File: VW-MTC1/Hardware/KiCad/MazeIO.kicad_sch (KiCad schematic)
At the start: 21 parts, among them J4 MAZE, Q4 AO3400A, U10 TPD4E05U06, U11 74LVC3G17

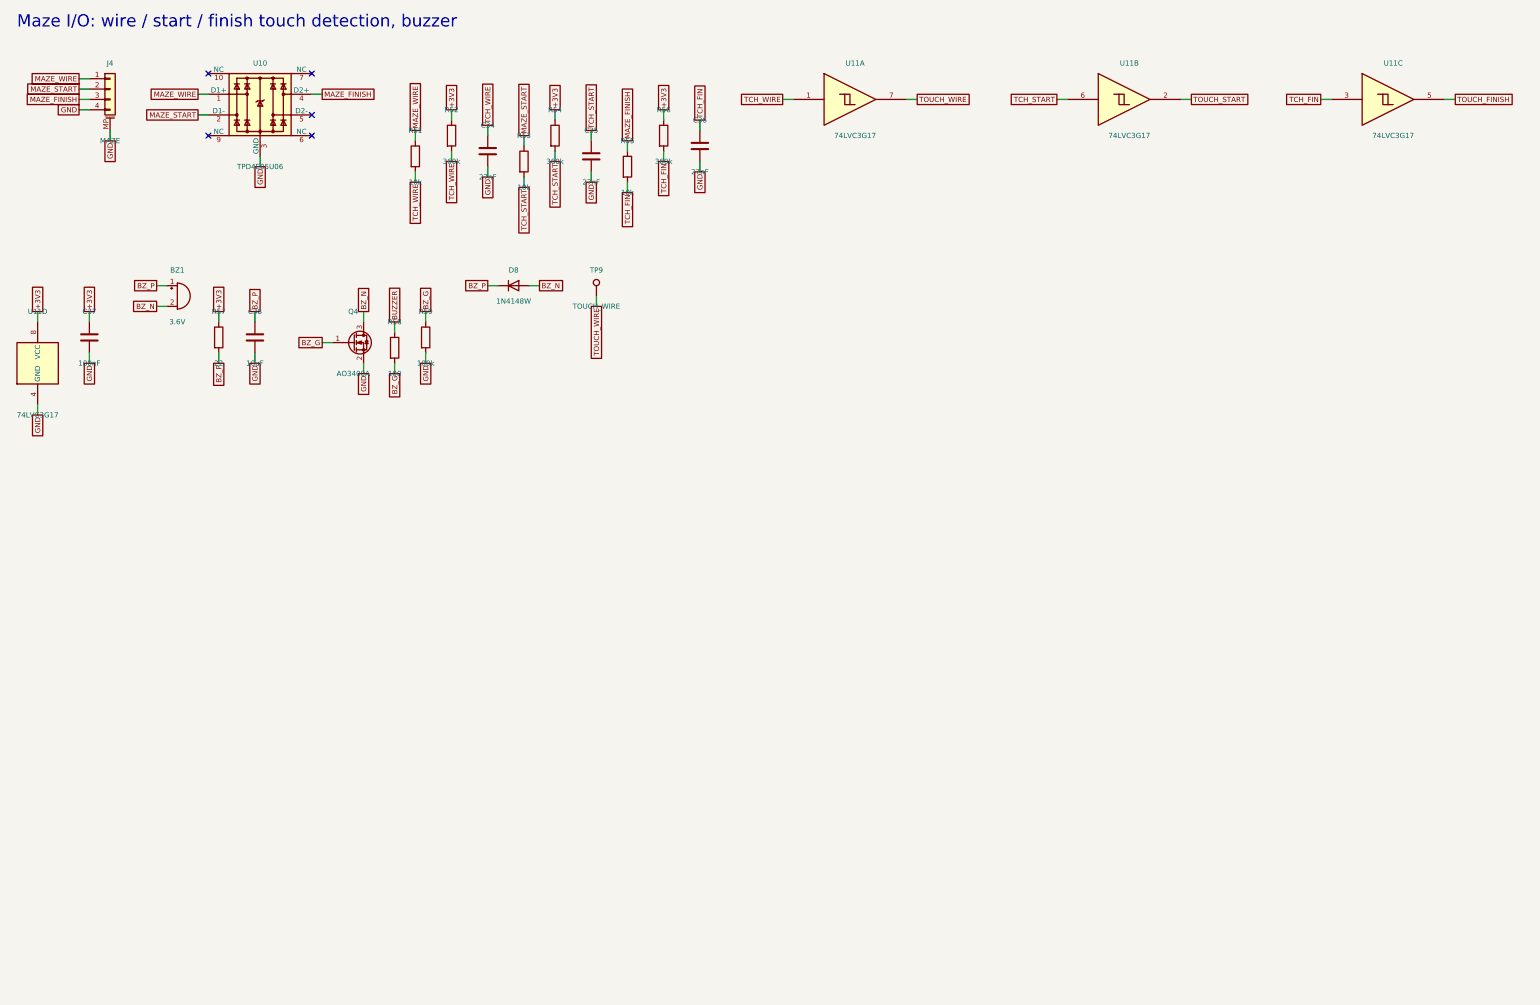
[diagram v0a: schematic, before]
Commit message: Apply Rev B touch circuit, routed PCB and topology-tested BOM
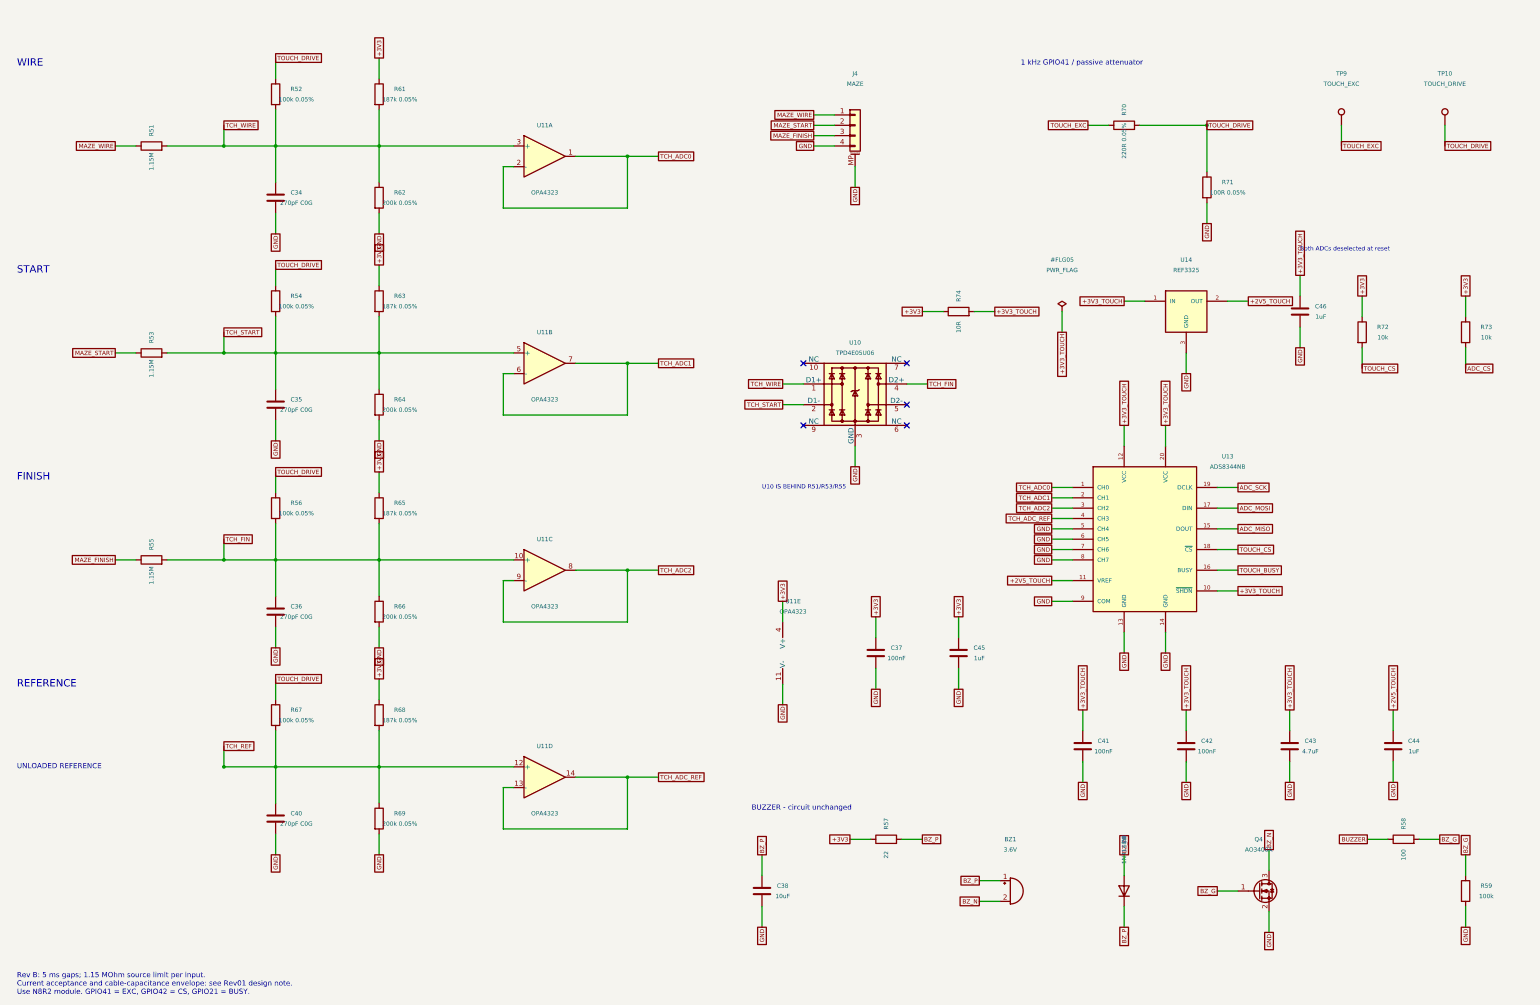
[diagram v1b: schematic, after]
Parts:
- removed U11: 74LVC3G17, Package_SO:VSSOP-8_2.3x2mm_P0.5mm, symbol 74xGxx:74LVC3G17
- added C40: 270pF C0G, Capacitor_SMD:C_0603_1608Metric, symbol Device:C
- added C41, C42: 100nF, Capacitor_SMD:C_0603_1608Metric, symbol Device:C
- added C43: 4.7uF, Capacitor_SMD:C_0603_1608Metric, symbol Device:C
- added C44, C45, C46: 1uF, Capacitor_SMD:C_0603_1608Metric, symbol Device:C
- added R61, R63, R65, R68: 187k 0.05%, Resistor_SMD:R_0603_1608Metric, symbol Device:R
- added R62, R64, R66, R69: 200k 0.05%, Resistor_SMD:R_0603_1608Metric, symbol Device:R
- added R67: 100k 0.05%, Resistor_SMD:R_0603_1608Metric, symbol Device:R
- added R70: 220R 0.05%, Resistor_SMD:R_0603_1608Metric, symbol Device:R
- added R71: 100R 0.05%, Resistor_SMD:R_0603_1608Metric, symbol Device:R
- added R72, R73: 10k, Resistor_SMD:R_0603_1608Metric, symbol Device:R
- added R74: 10R, Resistor_SMD:R_0603_1608Metric, symbol Device:R
- added TP10: TOUCH_DRIVE, TestPoint:TestPoint_Pad_D1.5mm, symbol Connector:TestPoint
- added U11: OPA4323, Package_SO:TSSOP-14_4.4x5mm_P0.65mm, symbol Voltwyn:OPA4323
- added U13: ADS8344NB, Package_SO:SSOP-20_5.3x7.2mm_P0.65mm, symbol Voltwyn:ADS8344NB
- added U14: REF3325, Package_TO_SOT_SMD:SOT-23, symbol Voltwyn:REF3325
- C34, C35, C36: value 27nF -> 270pF C0G; MPN GRM188R71H273KA01D -> GRM1885C1H271JA01D
- R51, R53, R55: value 10k -> 1.15M; MPN RC0603FR-0710kL -> RC0603FR-071M15L
- R52, R54, R56: value 360k -> 100k 0.05%; MPN RC0603FR-07360kL -> RG1608N-104-W-T1; Manufacturer Yageo -> Susumu
- TP9: value TOUCH_WIRE -> TOUCH_EXC
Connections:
- net +3V3: now also C45.1, R61.1, R63.1, R65.1, R68.1, R72.1, R73.1, R74.1, U11.4 (V+); no longer R52.1, R54.1, R56.1
- net GND: now also C40.2, C41.2, C42.2, C43.2, C44.2, C45.2, C46.2, R62.2, R64.2, R66.2, R69.2, R71.2, U11.11 (V-), U13.13 (GND), U13.14 (GND), U13.5 (CH4), U13.6 (CH5), U13.7 (CH6), U13.8 (CH7), U13.9 (COM), U14.3 (GND)
- net MAZE_FINISH: no longer U10.4 (D2+)
- net MAZE_START: no longer U10.2 (D1-)
- net MAZE_WIRE: no longer U10.1 (D1+)
- net TCH_FIN: now also U10.4 (D2+), R65.2, R66.1, U11.10 (+)
- net TCH_START: now also U10.2 (D1-), R63.2, R64.1, U11.5 (+)
- net TCH_WIRE: now also U10.1 (D1+), R61.2, R62.1, U11.3 (+)
- net TOUCH_WIRE renamed TOUCH_EXC
- net TOUCH_EXC: now also R70.1
- new net +2V5_TOUCH: C44.1, U13.11 (VREF), U14.2 (OUT)
- new net +3V3_TOUCH: C41.1, C42.1, C43.1, C46.1, R74.2, U13.10 (~{SHDN}), U13.12 (VCC), U13.20 (VCC), U14.1 (IN)
- new net ADC_CS: R73.2
- new net ADC_MISO: U13.15 (DOUT)
- new net ADC_MOSI: U13.17 (DIN)
- new net ADC_SCK: U13.19 (DCLK)
- new net TCH_ADC0: U11.1, U11.2 (-), U13.1 (CH0)
- new net TCH_ADC1: U11.6 (-), U11.7, U13.2 (CH1)
- new net TCH_ADC2: U11.8, U11.9 (-), U13.3 (CH2)
- new net TCH_ADC_REF: U11.13 (-), U11.14, U13.4 (CH3)
- new net TCH_REF: C40.1, R67.2, R68.2, R69.1, U11.12 (+)
- new net TOUCH_BUSY: U13.16 (BUSY)
- new net TOUCH_CS: R72.2, U13.18 (~{CS})
- new net TOUCH_DRIVE: R52.1, R54.1, R56.1, R67.1, R70.2, R71.1, TP10.1
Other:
- note added: "1 kHz GPIO41 / passive attenuator"
- note added: "BUZZER - circuit unchanged"
- note added: "Both ADCs deselected at reset"
- note added: "FINISH"
- note added: "REFERENCE"
- note added: "Rev B: 5 ms gaps; 1.15 MOhm source limit per input. Current acceptance and cable-capacitance envelope: see Rev01 design note. Use N8R2 module. GPIO41 = EXC, GPIO42 = CS, GPIO21 = BUSY."
- note added: "START"
- note added: "U10 IS BEHIND R51/R53/R55"
- note added: "UNLOADED REFERENCE"
- note added: "WIRE"
- note removed: "Maze I/O: wire / start / finish touch detection, buzzer"
- title: Maze I/O: wire / start / finish touch detection, buzzer -> Synchronous touch acquisition and buzzer
- moved on the sheet: BZ1, C34, C35, C36, C37, C38, D8, J4, Q4, R51, R52, R53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
